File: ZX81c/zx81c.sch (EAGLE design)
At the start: 72 parts, among them IC1 ZX81ULA, IC2 27C512, IC2B ZXROM-SMALL, IC3 Z80CPU, IC4 62256, IC4A 2114, IC4B 2114, K1 ZX81CONN, K2 MIC, K3 EAR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

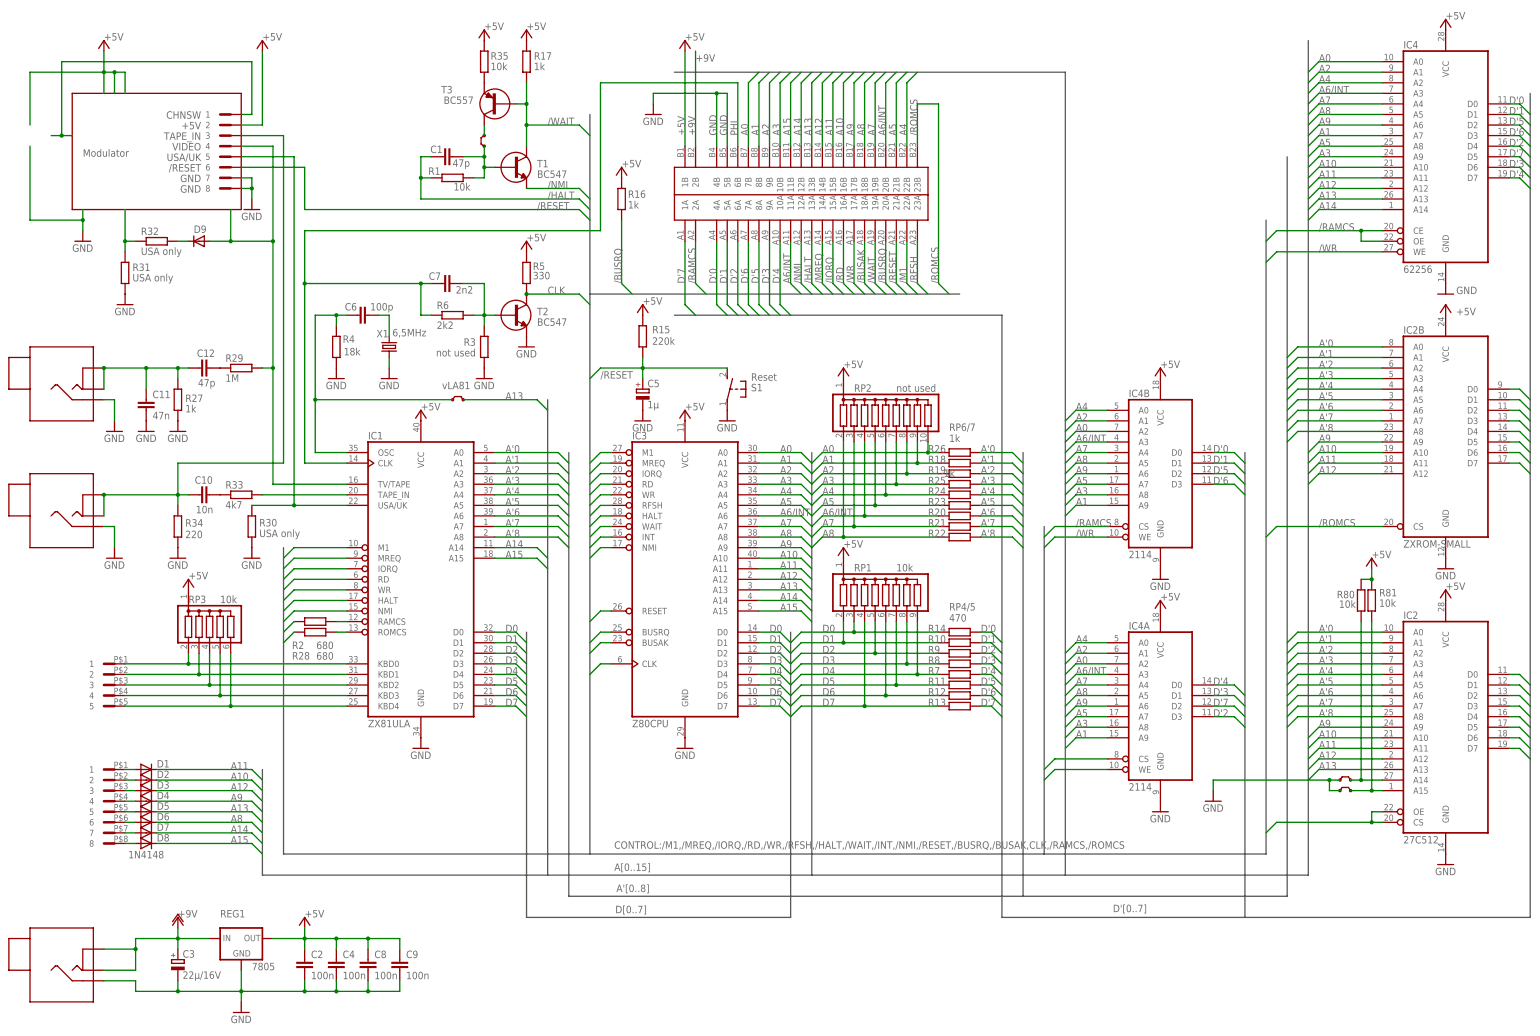
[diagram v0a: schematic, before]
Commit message: Add files via upload
Changed connectors to 4 pin version. Corrected Issue 3 C string and added a year
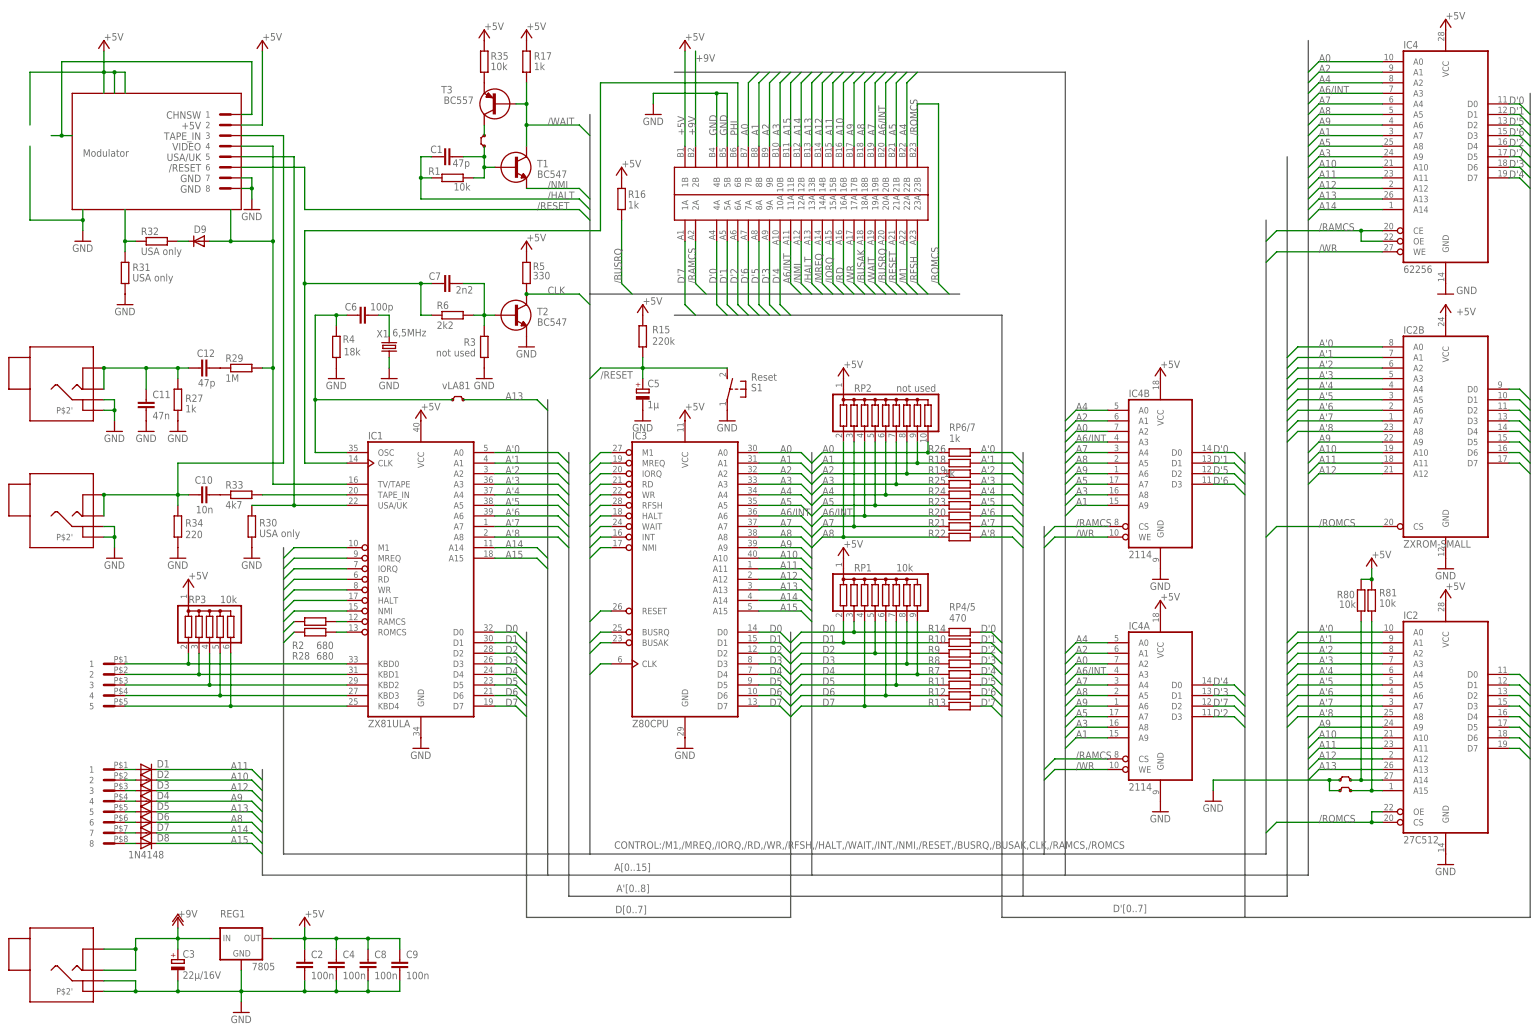
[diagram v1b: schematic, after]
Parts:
- K2, K3, K4: device sinclair:ZXKLINKE -> sinclair:ZXKLINKE4POL
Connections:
- net GND: now also K2.P$2', K3.P$2', K4.P$2'
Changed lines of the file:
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@@
 <part name="KB1" library="sinclair" deviceset="ZXKBD5CON" device=""/>
 <part name="KB2" library="sinclair" deviceset="ZXKBD8CON" device=""/>
-<part name="K4" library="sinclair" deviceset="ZXKLINKE" device="" value="DCIN"/>
-<part name="K3" library="sinclair" deviceset="ZXKLINKE" device="" value="EAR"/>
-<part name="K2" library="sinclair" deviceset="ZXKLINKE" device="" value="MIC"/>
+<part name="K4" library="sinclair" deviceset="ZXKLINKE4POL" device="" value="DCIN"/>
+<part name="K3" library="sinclair" deviceset="ZXKLINKE4POL" device="" value="EAR"/>
+<part name="K2" library="sinclair" deviceset="ZXKLINKE4POL" device="" value="MIC"/>
 <part name="U$38" library="sinclair" deviceset="GND" device=""/>
 <part name="U$39" library="sinclair" deviceset="GND" device=""/>
@@
 <wire x1="40.64" y1="17.78" x2="40.64" y2="15.24" width="0.1524" layer="91"/>
 <wire x1="40.64" y1="15.24" x2="50.8" y2="15.24" width="0.1524" layer="91"/>
+<pinref part="K4" gate="G$1" pin="P$2'"/>
+<wire x1="33.02" y1="15.24" x2="40.64" y2="15.24" width="0.1524" layer="91"/>
+<junction x="40.64" y="15.24"/>
 </segment>
 <segment>
@@
 <pinref part="K3" gate="G$1" pin="P$2"/>
 <wire x1="33.02" y1="127" x2="35.56" y2="127" width="0.1524" layer="91"/>
-<wire x1="35.56" y1="127" x2="35.56" y2="121.92" width="0.1524" layer="91"/>
+<wire x1="35.56" y1="127" x2="35.56" y2="124.46" width="0.1524" layer="91"/>
+<pinref part="K3" gate="G$1" pin="P$2'"/>
+<wire x1="35.56" y1="124.46" x2="35.56" y2="121.92" width="0.1524" layer="91"/>
+<wire x1="33.02" y1="124.46" x2="35.56" y2="124.46" width="0.1524" layer="91"/>
+<junction x="35.56" y="124.46"/>
 </segment>
 <segment>
@@
 <pinref part="K2" gate="G$1" pin="P$2"/>
 <wire x1="33.02" y1="157.48" x2="35.56" y2="157.48" width="0.1524" layer="91"/>
-<wire x1="35.56" y1="157.48" x2="35.56" y2="152.4" width="0.1524" layer="91"/>
+<wire x1="35.56" y1="157.48" x2="35.56" y2="154.94" width="0.1524" layer="91"/>
+<pinref part="K2" gate="G$1" pin="P$2'"/>
+<wire x1="35.56" y1="154.94" x2="35.56" y2="152.4" width="0.1524" layer="91"/>
+<wire x1="33.02" y1="154.94" x2="35.56" y2="154.94" width="0.1524" layer="91"/>
+<junction x="35.56" y="154.94"/>
 </segment>
 <segment>
@@
 <wire x1="274.32" y1="68.58" x2="261.62" y2="68.58" width="0.1524" layer="91"/>
 <wire x1="261.62" y1="68.58" x2="259.08" y2="66.04" width="0.1524" layer="91"/>
+<label x="266.7" y="68.58" size="1.778" layer="95"/>
 </segment>
 <segment>
@@
 <wire x1="274.32" y1="71.12" x2="261.62" y2="71.12" width="0.1524" layer="91"/>
 <wire x1="261.62" y1="71.12" x2="259.08" y2="68.58" width="0.1524" layer="91"/>
+<label x="266.7" y="71.12" size="1.778" layer="95"/>
 </segment>
 <segment>
@@
 <wire x1="340.36" y1="55.88" x2="337.82" y2="55.88" width="0.1524" layer="91"/>
 <junction x="337.82" y="55.88"/>
-</segment>
-</net>
+<label x="325.12" y="55.88" size="1.778" layer="95"/>
+</segment>
+</net>
